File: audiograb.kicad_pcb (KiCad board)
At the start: 4 copper layers, 165.2 x 72 mm, 143 parts, among them IC1 USB2244I-AEZG-06, J1 USB_C_Receptacle_USB2.0_16P, J10 20579-001E, J11 732511150, J12 732511150, J13 732511150, J14 732511150, J15 F32Q-1A7H1-11022, J16 MEM2075-00-140-01-A, J17 3V5_out, J2 SAM10346-ND, J3 SAM10346-ND, J4 JST-PH, J5 12V_in, J6 20579-001E, J7 20579-001E, J8 20579-001E, J9 M.2_Socket_B, M1 ComputeModule5-CM5, P1 SF72S006VBDR2500, Q1 Q_PMOS_GSD, Q2 DMT6007LFG-7, Q3 NX3008NBKW_115, SW1 1825910-6, U1 LMR51450SDRRR, U10 CD4043BDR, U11 TPS22919DCKR, U12 IP4220CZ6F, U2 LM74700QDBVTQ1, U3 LMR51450SDRRR, U8 MAX4996LETG_

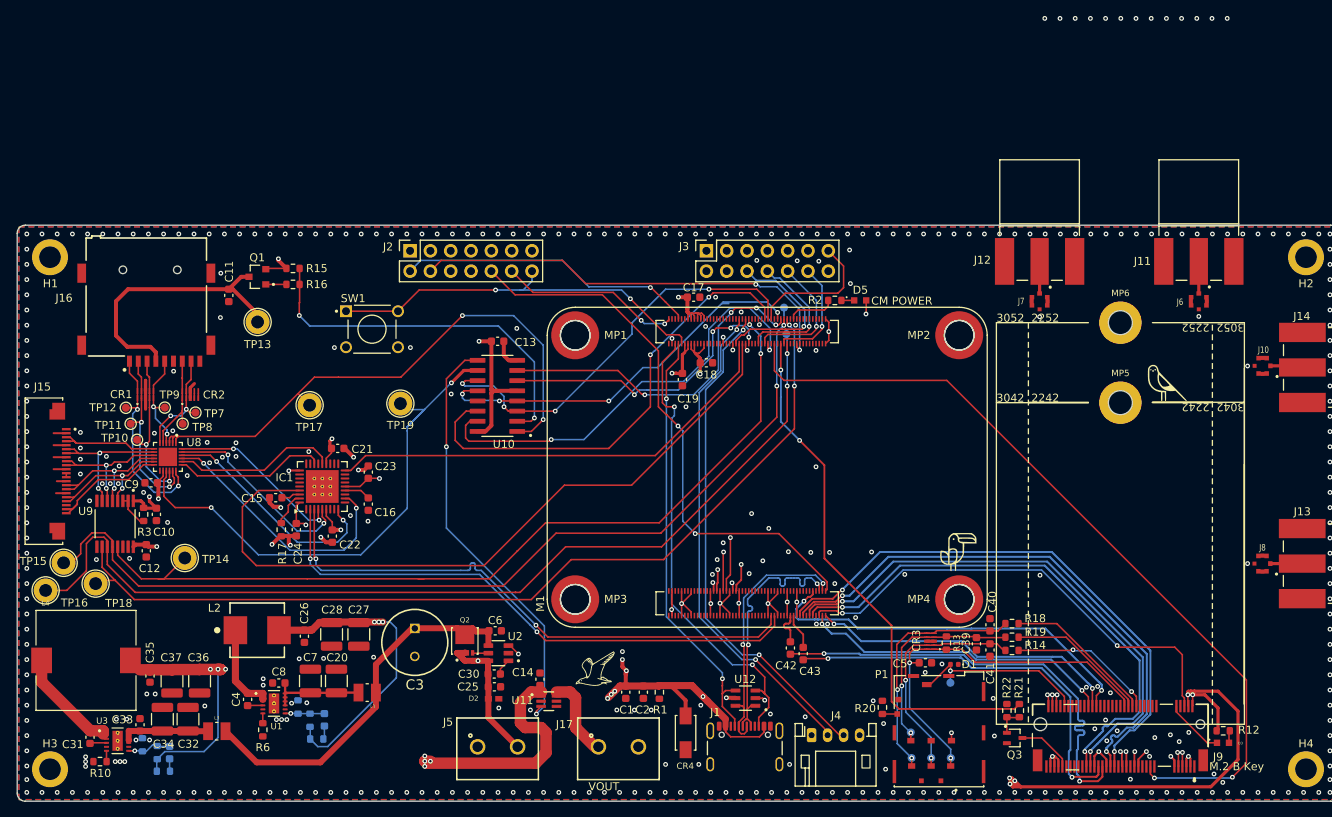
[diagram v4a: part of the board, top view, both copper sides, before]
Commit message: Må justere impedans for USB og PCIE, så er vi gtg
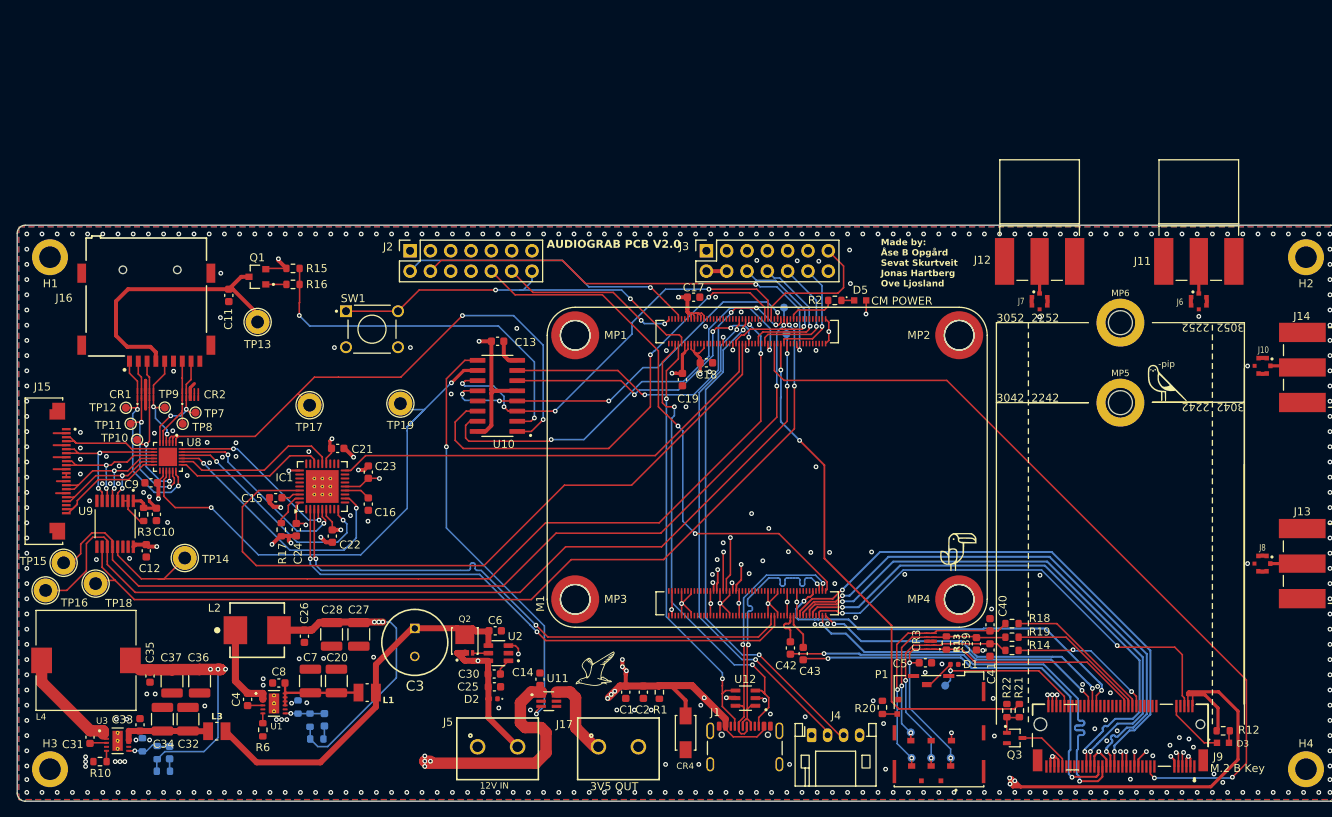
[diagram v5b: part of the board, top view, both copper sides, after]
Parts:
- C1: value 100n -> 100nF
- C10, C12, C18, C19: value 0.1uF -> 100nF
- C13, C17, C9: value 0.1uF ceramic -> 100nF
- C15, C16: value 1.0 µ -> 1uF
- C2: value 100n -> 100F
- D1: value D_TVS -> 0402ESDA-MLP1
- D2: footprint 0402ESDA-MLP1:ESD_0402ESDA-MLP1 -> Diode_SMD:D_0402_1005Metric
- U9: value ~ -> SN74AVCH4T245PW
- moved G*** 54.9 mm to (185.7, 94.8)
- moved TP1 0.74 mm to (145.8, 97.5)
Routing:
- net +3V3_CM5: track 359.9 -> 356.4 mm
- net +5V: track 175.1 -> 177.9 mm
- net /SD_SWITCH_DISABLE: track 49.6 -> 48.7 mm
- net /SD2: track 109.0 -> 108.3 mm
- net /modem/USIM1_DET: track 23.3 -> 23.9 mm
- net +3V5: track 245.6 -> 245.0 mm, vias 15 -> 13
- net GND: track 92.8 -> 92.5 mm, vias 407 -> 397
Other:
- board text added: "-pip"
- board text added: "12V IN"
- board text added: "3V5 OUT"
- board text added: "AUDIOGRAB PCB V2.0"
- board text added: "Made by: Åse B Opgård Sevat Skurtveit Jonas Hartberg Ove Ljosland"
- board text removed: "AUDIOGRAB PCB V2.0 Åse B Opgård Sevat Skurtveit Jonas Hartberg Ove Ljosland"
- board text removed: "VOUT"

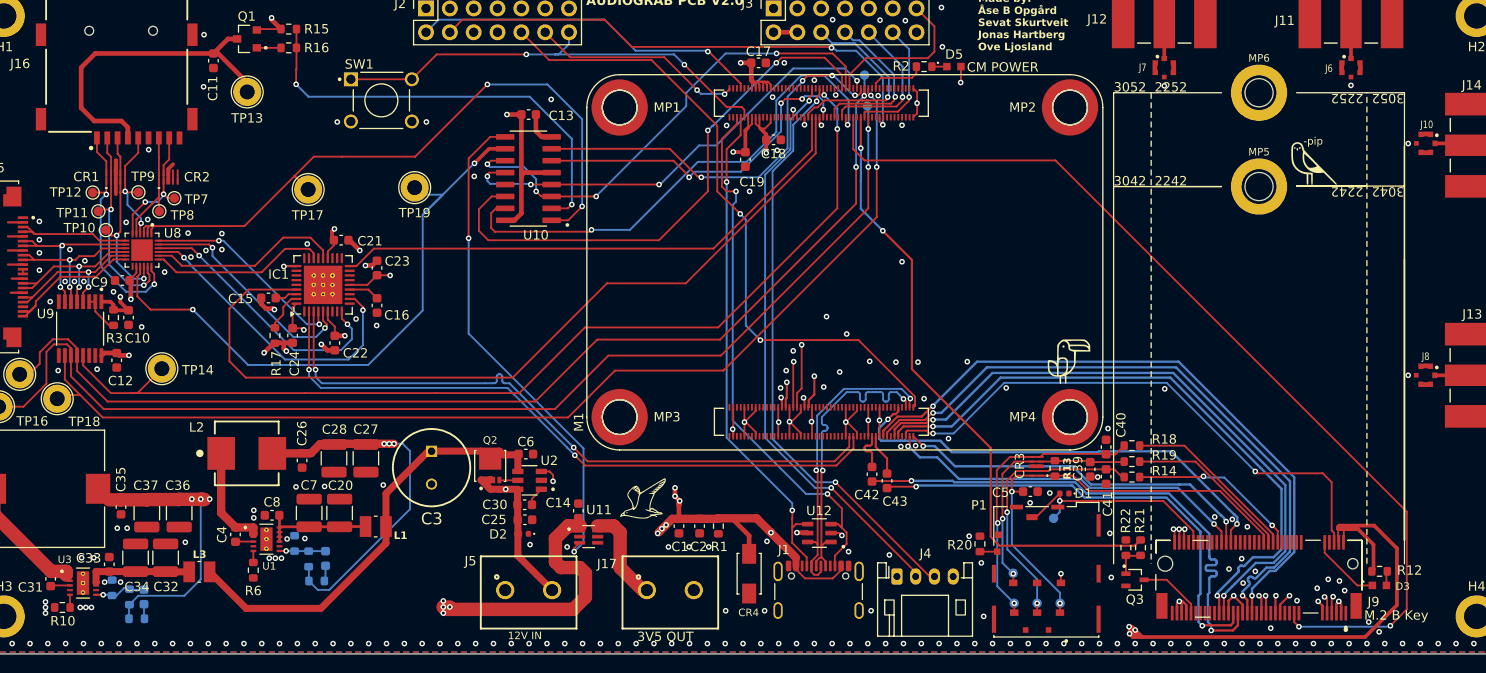
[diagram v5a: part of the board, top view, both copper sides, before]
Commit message: added copper pour on power plane and increaced clearnace from 0.2 to 0.5
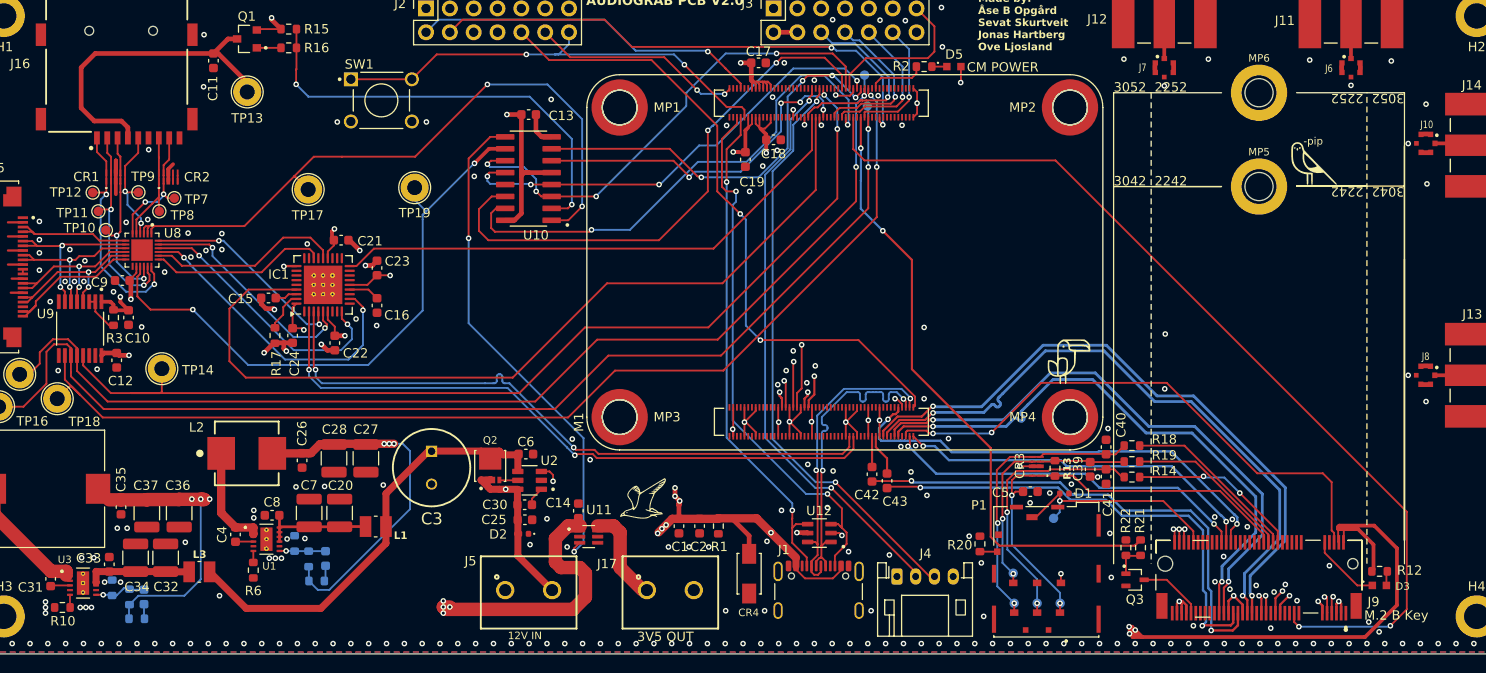
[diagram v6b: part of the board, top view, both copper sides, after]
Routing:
- net /USB3-1-RX_N: track 79.6 -> 92.2 mm
- net /USB3-1-RX_P: track 79.6 -> 92.0 mm
- net GND: track 92.5 -> 98.5 mm, vias 397 -> 412
- net /USB3-1-TX_N: track 84.2 -> 90.1 mm
- net /USB3-1-D_P: track 87.8 -> 93.3 mm
- net /PCIE_CLK_P: track 66.7 -> 61.5 mm
- net /PCIE_CLK_N: track 67.3 -> 62.2 mm
- net /USB3-1-TX_P: track 83.7 -> 88.5 mm
- net /USB3-1-D_N: track 87.9 -> 92.1 mm
- net Net-(U10-Q3): track 67.7 -> 64.1 mm
- net /modem/PCIE_RX_MOD_N: track 56.3 -> 53.4 mm
- net /GPCLK: track 90.5 -> 92.8 mm
- net /PCIE_TX_N: track 4.42 -> 3.27 mm
- net /PCIE_RX_N: track 69.4 -> 68.5 mm
- net /PCIE_RX_P: track 68.8 -> 67.9 mm
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- added copper zone on In2.Cu, net GND

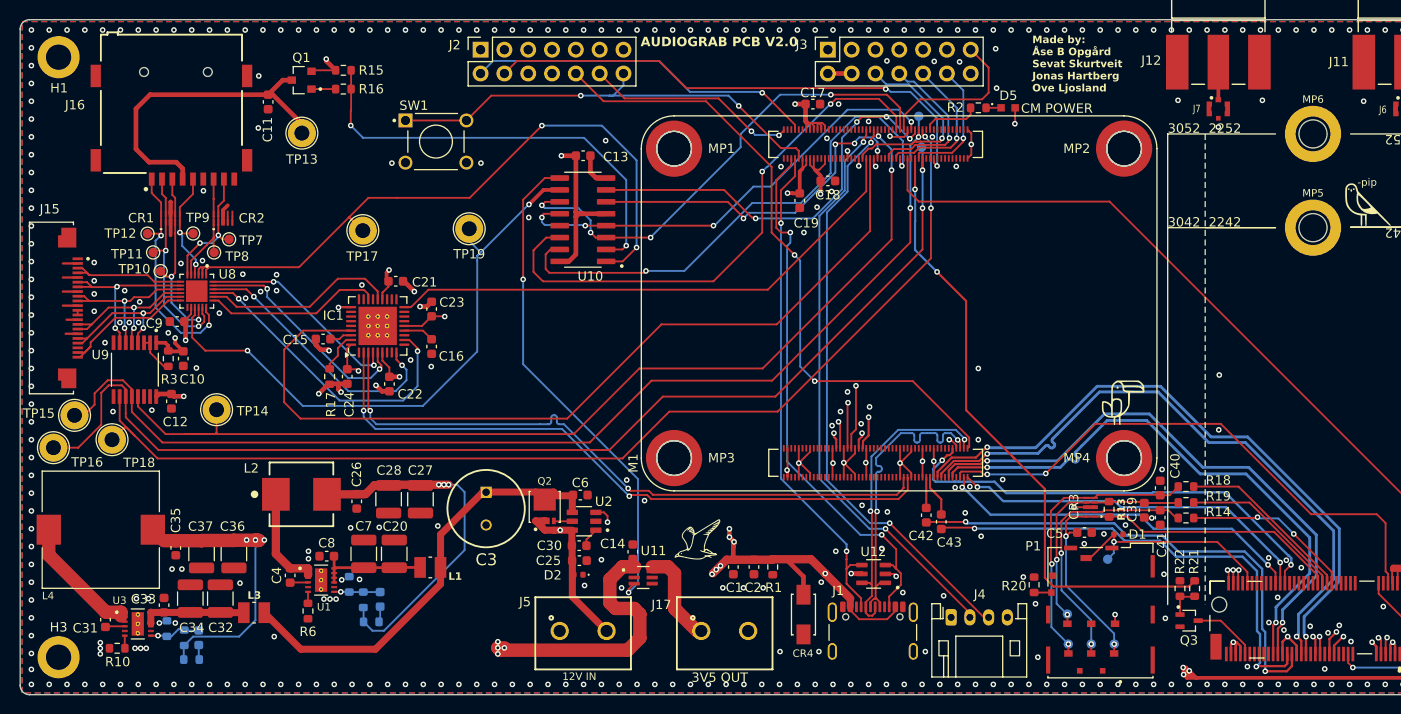
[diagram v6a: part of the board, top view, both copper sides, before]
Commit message: changed sd lines impedanc etc. power plane zone 3.3v
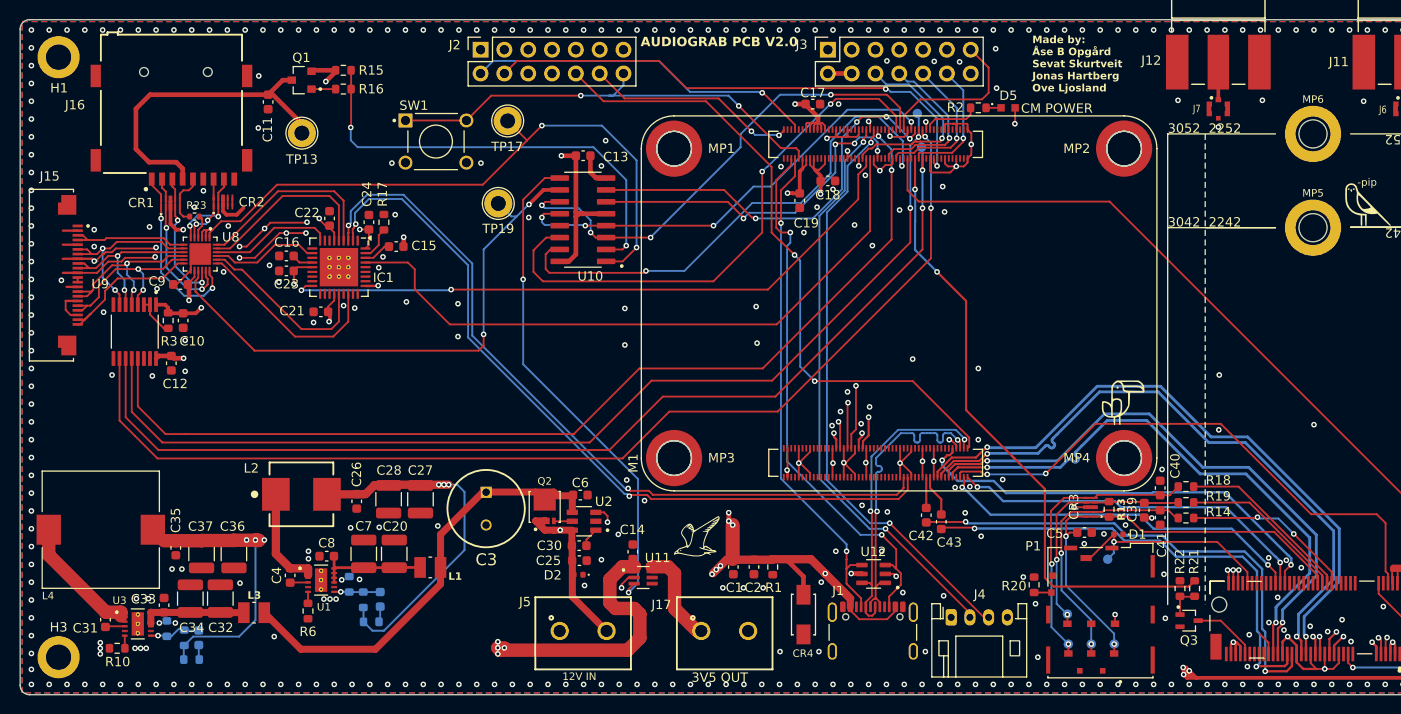
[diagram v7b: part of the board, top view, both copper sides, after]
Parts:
- removed TP10, TP11, TP12, TP7, TP8, TP9: TestPoint, TestPoint:TestPoint_Pad_D1.0mm
- removed TP14, TP15, TP16, TP18: TestPoint, TestPoint:TestPoint_Loop_D2.60mm_Drill1.6mm_Beaded
- added R23: 33, Resistor_SMD:R_0402_1005Metric, F.Cu at (48.4, 61.0)
- moved TP17 19.4 mm to (81.8, 50.8)
- moved C22 18.8 mm to (62.8, 61.2), turned to 90 degrees
- moved C16 18.3 mm to (58.2, 65.2), turned to 180 degrees
- moved R17 17.5 mm to (68.6, 61.6), turned to -90 degrees
- moved C24 16.6 mm to (67.0, 61.6), turned to -90 degrees
- moved C23 16.0 mm to (58.2, 66.8), turned to 180 degrees
- moved C15 12.6 mm to (69.9, 64.2), turned to 180 degrees
- moved C21 8.63 mm to (61.9, 71.2), turned to 180 degrees
- moved IC1 7.51 mm to (63.8, 66.4), turned to -90 degrees
- moved TP19 4.11 mm to (80.8, 59.6)
- moved C10 4.06 mm to (47.2, 72.1)
- moved C12 4.06 mm to (45.9, 76.6)
- moved R3 4.06 mm to (45.6, 72.1)
- moved U9 4.06 mm to (42.0, 73.3)
- moved C9 3.97 mm to (46.9, 68.2)
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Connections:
- net Net-(J16-CD/DAT3) renamed /sd-interface/sd_card_2
- net Net-(J16-CMD) renamed /sd-interface/sd_card_3
- net Net-(J16-DAT0) renamed /sd-interface/sd_card_7
- net Net-(J16-DAT1) renamed /sd-interface/sd_card_8
- net Net-(J16-DAT2) renamed /sd-interface/sd_card1
- U1 pad 14: GND -> (no net)
- U1 pad 15: GND -> (no net)
- U1 pad 16: GND -> (no net)
- U3 pad 14: GND -> (no net)
- U3 pad 15: GND -> (no net)
- U3 pad 16: GND -> (no net)
- U8 pad 4: Net-(J16-CLK) -> /sd-interface/sd_card_5
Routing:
- net GND: track 98.5 -> 170.6 mm, vias 412 -> 431
- net /GPCLK: track 92.8 -> 69.6 mm
- net /sd-interface/SD-pin3: track 33.1 -> 11.7 mm, vias 2 -> 0
- net /sd-interface/SD-pin5: track 29.0 -> 13.2 mm, vias 2 -> 0
- net /USB3-0-D_P: track 70.4 -> 82.4 mm
- net /USB3-0-D_N: track 70.2 -> 82.2 mm
- net /USB_INT_RESET: track 57.9 -> 69.4 mm, vias 0 -> 2
- net /SD5: track 123.1 -> 113.8 mm
- net +3V3_CM5: track 356.4 -> 347.6 mm
- net Net-(J16-CLK): track 13.0 -> 5.66 mm, vias 2 -> 0
- net /sd-interface/sd_card1: track 25.1 -> 19.3 mm
- net /sd-interface/sd_card_2: track 22.4 -> 16.8 mm
- net /SD3: track 119.0 -> 113.6 mm
- net /sd-interface/SD-pin7: track 24.9 -> 19.6 mm, vias 2 -> 0
- net /sd-interface/sd_card_7: track 13.1 -> 7.81 mm, vias 0 -> 2
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- added copper zone on In2.Cu, net +3V3_CM5
